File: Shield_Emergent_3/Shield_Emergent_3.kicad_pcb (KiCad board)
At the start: 4 copper layers, 23.6 x 33.4 mm, 17 parts, among them J1 USB3_B_Micro, J2 Conn_02x03_Odd_Even, J3 USB3_B_Micro, U3 SP3012-06UTG, U4 SP3012-06UTG, X1 USB_C_24pins

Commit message: v1.5 some DRC errors were corrected
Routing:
- net VBUS: track 23.1 -> 42.8 mm, vias 1 -> 2
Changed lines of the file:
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@@
 		(tags "resistor")
 		(property "Reference" "R1"
-			(at 0.4 -1.6 360)
+			(at 0.4 -1.6 0)
 			(layer "F.SilkS")
 			(effects
@@
 		)
 		(property "Value" "0"
-			(at -1 -0.8 360)
+			(at -1 -0.8 0)
 			(layer "F.Fab")
 			(effects
@@
 		)
 		(fp_text user "${REFERENCE}"
-			(at 0 0 270)
+			(at 0 0 -90)
 			(layer "F.Fab")
 			(effects
@@
 	)
 	(segment
+		(start 13.575 31.175)
+		(end 13.2 30.8)
+		(width 0.25)
+		(layer "F.Cu")
+		(net 3)
+	)
+	(segment
 		(start 11.4 17.6)
 		(end 11.85 18.05)
@@
 	)
 	(segment
+		(start 16.95 18.05)
+		(end 20.2 18.05)
+		(width 0.25)
+		(layer "F.Cu")
+		(net 3)
+	)
+	(segment
+		(start 20.2 27.104595)
+		(end 16.129595 31.175)
+		(width 0.25)
+		(layer "F.Cu")
+		(net 3)
+	)
+	(segment
 		(start 16.95 15.55)
 		(end 13.45 15.55)
@@
 	)
 	(segment
-		(start 16.95 18.05)
+		(start 16.129595 31.175)
+		(end 13.575 31.175)
+		(width 0.25)
+		(layer "F.Cu")
+		(net 3)
+	)
+	(segment
+		(start 20.2 18.05)
+		(end 20.2 27.104595)
+		(width 0.25)
+		(layer "F.Cu")
+		(net 3)
+	)
+	(segment
+		(start 20.2 18.05)
 		(end 20.35 18.05)
 		(width 0.25)
@@
 		(net 3)
 	)
+	(via
+		(at 13.2 30.8)
+		(size 0.6)
+		(drill 0.3)
+		(layers "F.Cu" "B.Cu")
+		(net 3)
+	)
 	(segment
 		(start 22.054522 16.317022)
@@
 	)
 	(segment
+		(start 11.4625 30.8)
+		(end 11.4 30.7375)
+		(width 0.25)
+		(layer "B.Cu")
+		(net 3)
+	)
+	(segment
 		(start 21 17.4)
 		(end 21.5375 17.4)
@@
 		(layer "B.Cu")
 		(net 3)
+	)
+	(segment
+		(start 13.2 30.8)
+		(end 11.4625 30.8)
+		(width 0.25)
+		(layer "B.Cu")
+		(net 3)

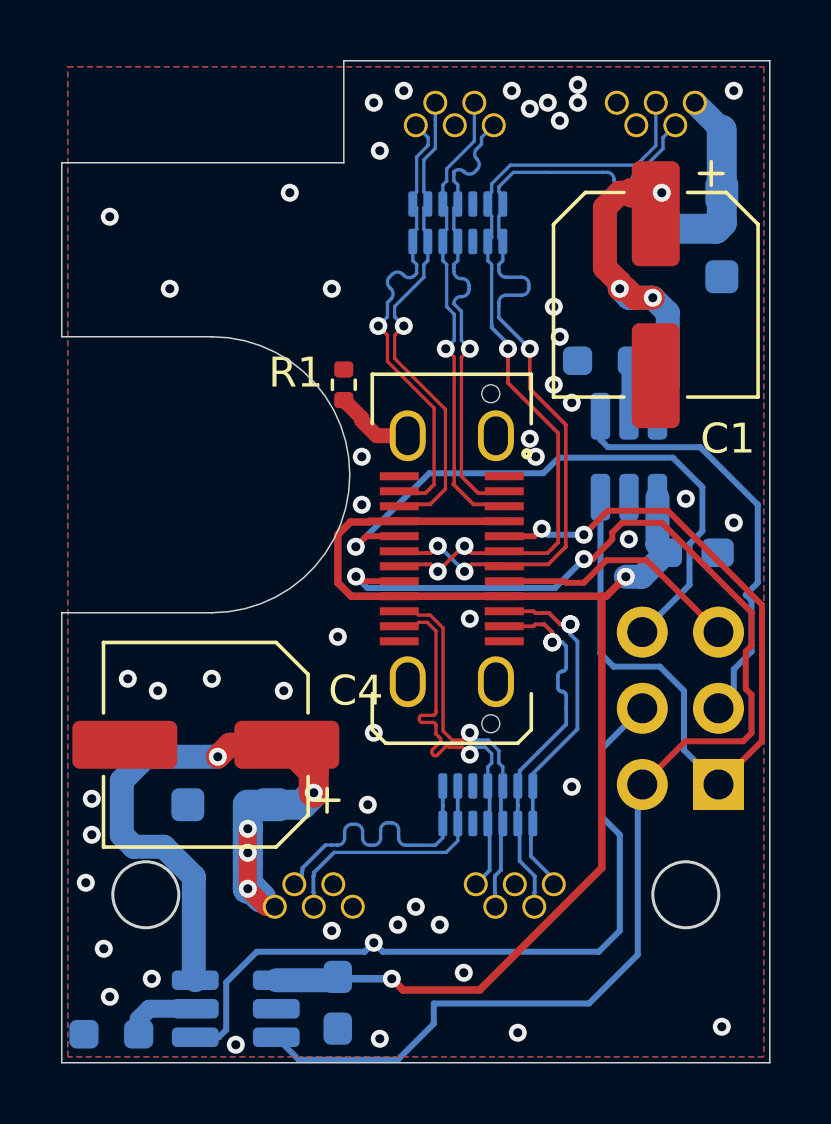
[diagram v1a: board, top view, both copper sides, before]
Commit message: v1.6 routing is nearly completed
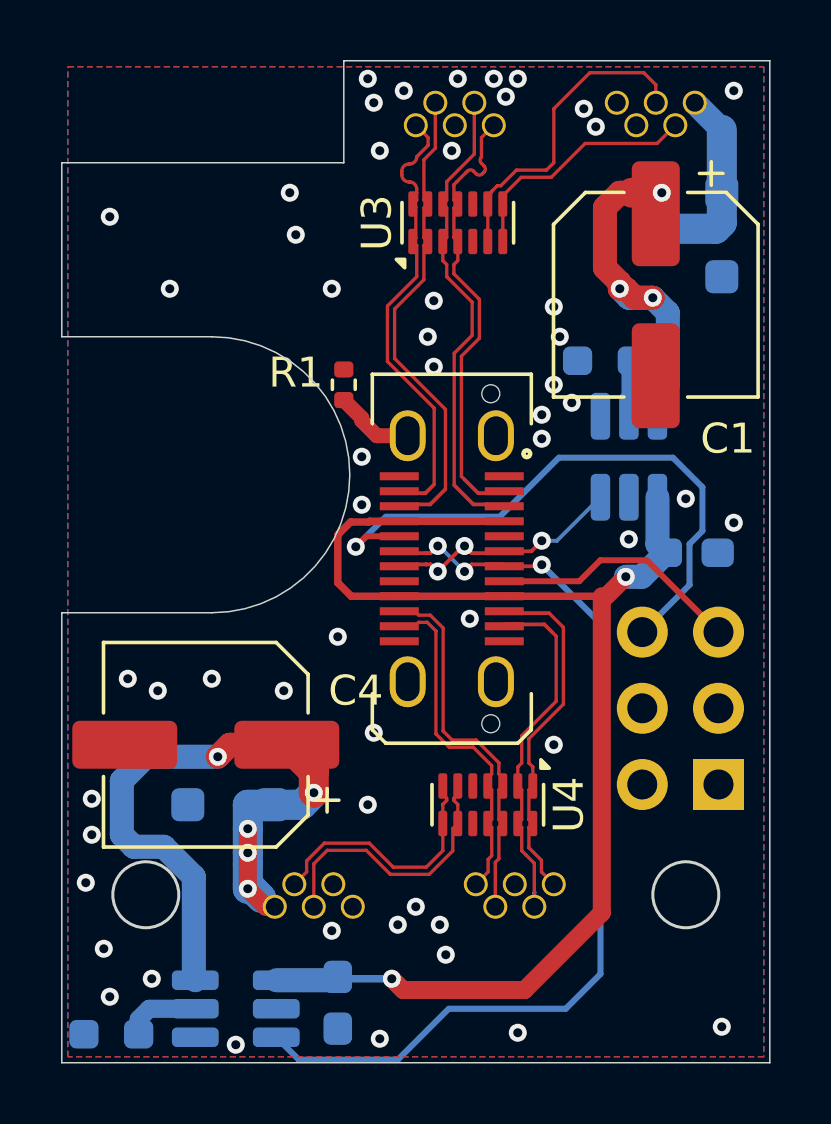
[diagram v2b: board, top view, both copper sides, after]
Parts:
- U3, U4: moved to F.Cu
- turned U3 to 90 degrees
- turned U4 to -90 degrees
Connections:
- J2 pad 1: EN1 -> unconnected-(J2-Pin_1-Pad1)
- J2 pad 2: EN2 -> unconnected-(J2-Pin_2-Pad2)
- J2 pad 3: nFLT1 -> unconnected-(J2-Pin_3-Pad3)
- J2 pad 4: nFLT2 -> unconnected-(J2-Pin_4-Pad4)
- X1 pad A5: EN1 -> unconnected-(X1-CC1-PadA5)
- X1 pad A6: D+ -> EN1
- X1 pad A7: D- -> EN2
- X1 pad B5: EN2 -> unconnected-(X1-CC2-PadB5)
- X1 pad B6: D+ -> EN1
- X1 pad B7: D- -> EN2
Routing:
- net nFLT2: track 25.0 -> 0.00 mm, vias 1 -> 0
- net EN1: track 29.1 -> 8.65 mm, vias 2 -> 3
- net D-: track 28.6 -> 8.25 mm, vias 3 -> 0
- net D+: track 26.6 -> 10.7 mm, vias 3 -> 0
- net nFLT1: track 14.4 -> 0.00 mm
- net EN2: track 45.6 -> 32.7 mm, vias 2 -> 3
- net TX2+: track 14.3 -> 11.6 mm, vias 1 -> 0
- net RX2+: track 13.8 -> 11.8 mm, vias 2 -> 0
- net RX2-: track 13.8 -> 12.3 mm, vias 2 -> 0
- net 2_D-: track 9.72 -> 8.56 mm
- net 2_D+: track 8.29 -> 9.24 mm
- net VBUS: track 42.8 -> 43.7 mm
- net TX2-: track 13.4 -> 12.6 mm, vias 1 -> 0
- net unconnected-(J2-Pin_3-Pad3): track 0.00 -> 0.72 mm
- net RX1+: track 15.8 -> 15.4 mm, vias 1 -> 0
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
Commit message: v1.7 Keyboard connector was added, decomposed and routed
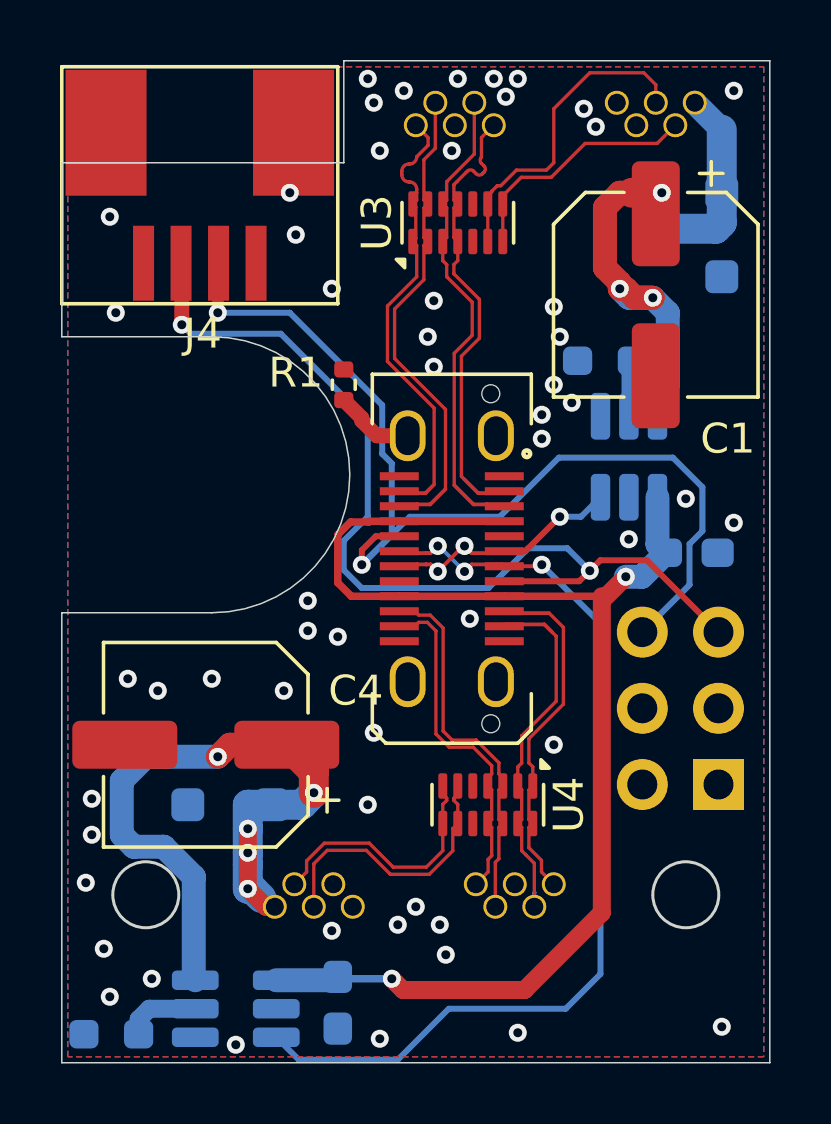
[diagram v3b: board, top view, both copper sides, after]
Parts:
- added J4: Conn_01x05_Socket, myLib8:04FFS-SP-TF (LF)(SN), F.Cu at (6.80, 2.60)
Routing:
- net BTN1: track 8.42 -> 32.6 mm, vias 0 -> 2
- net BTN2: track 20.4 -> 35.1 mm, vias 1 -> 2

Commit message: v1.8 ESD protection 4 buttons was added
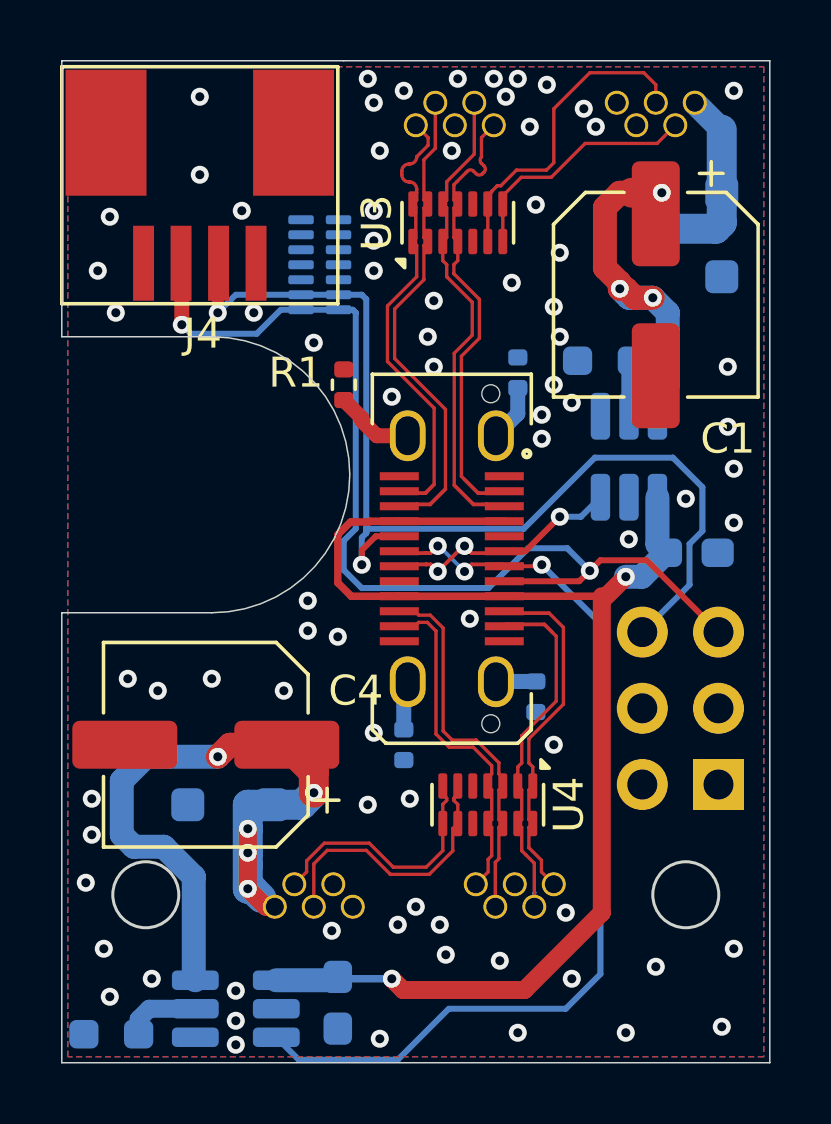
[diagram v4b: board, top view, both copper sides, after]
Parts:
- added R2: 0, Resistor_SMD:R_0402_1005Metric, B.Cu at (17.4, 10.6)
- added R3: 0, Resistor_SMD:R_0402_1005Metric, B.Cu at (13.6, 23.0)
- added R5: 0, Resistor_SMD:R_0402_1005Metric, B.Cu at (18.0, 21.4)
- added U5: SP3012-06UTG, myLib8:DFN-14_1.35x3.5mm_P0.5mm, B.Cu at (10.8, 7.00)
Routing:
- net Shield: track 2.68 -> 7.55 mm
- net BTN1: track 32.6 -> 34.8 mm
- net BTN2: track 35.1 -> 36.2 mm
- net GND: vias 55 -> 79
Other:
- outline, holes or cut-outs redrawn

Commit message: v1.9 Ordered version was added
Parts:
- moved R8 1.25 mm to (4.60, 31.6), turned to -90 degrees
- moved R1 0.76 mm to (11.7, 10.2)
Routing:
- net VBUS: track 43.7 -> 42.7 mm
